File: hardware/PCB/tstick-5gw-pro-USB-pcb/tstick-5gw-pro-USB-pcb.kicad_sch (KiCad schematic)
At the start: 52 parts, among them J1 USB_C_Receptacle_USB2.0, J2 GPIO2, J3 GPIO1, Q2 20V/4.2A/52mOhm/1.4W, Q3 BSS138, SW1 JST-SH-1.00mm 1x2, SW2 PTS810 SJM Switch, U1 XC6222B331MR-G, U3 MCP73831-2-OT, U4 PCA9306DP

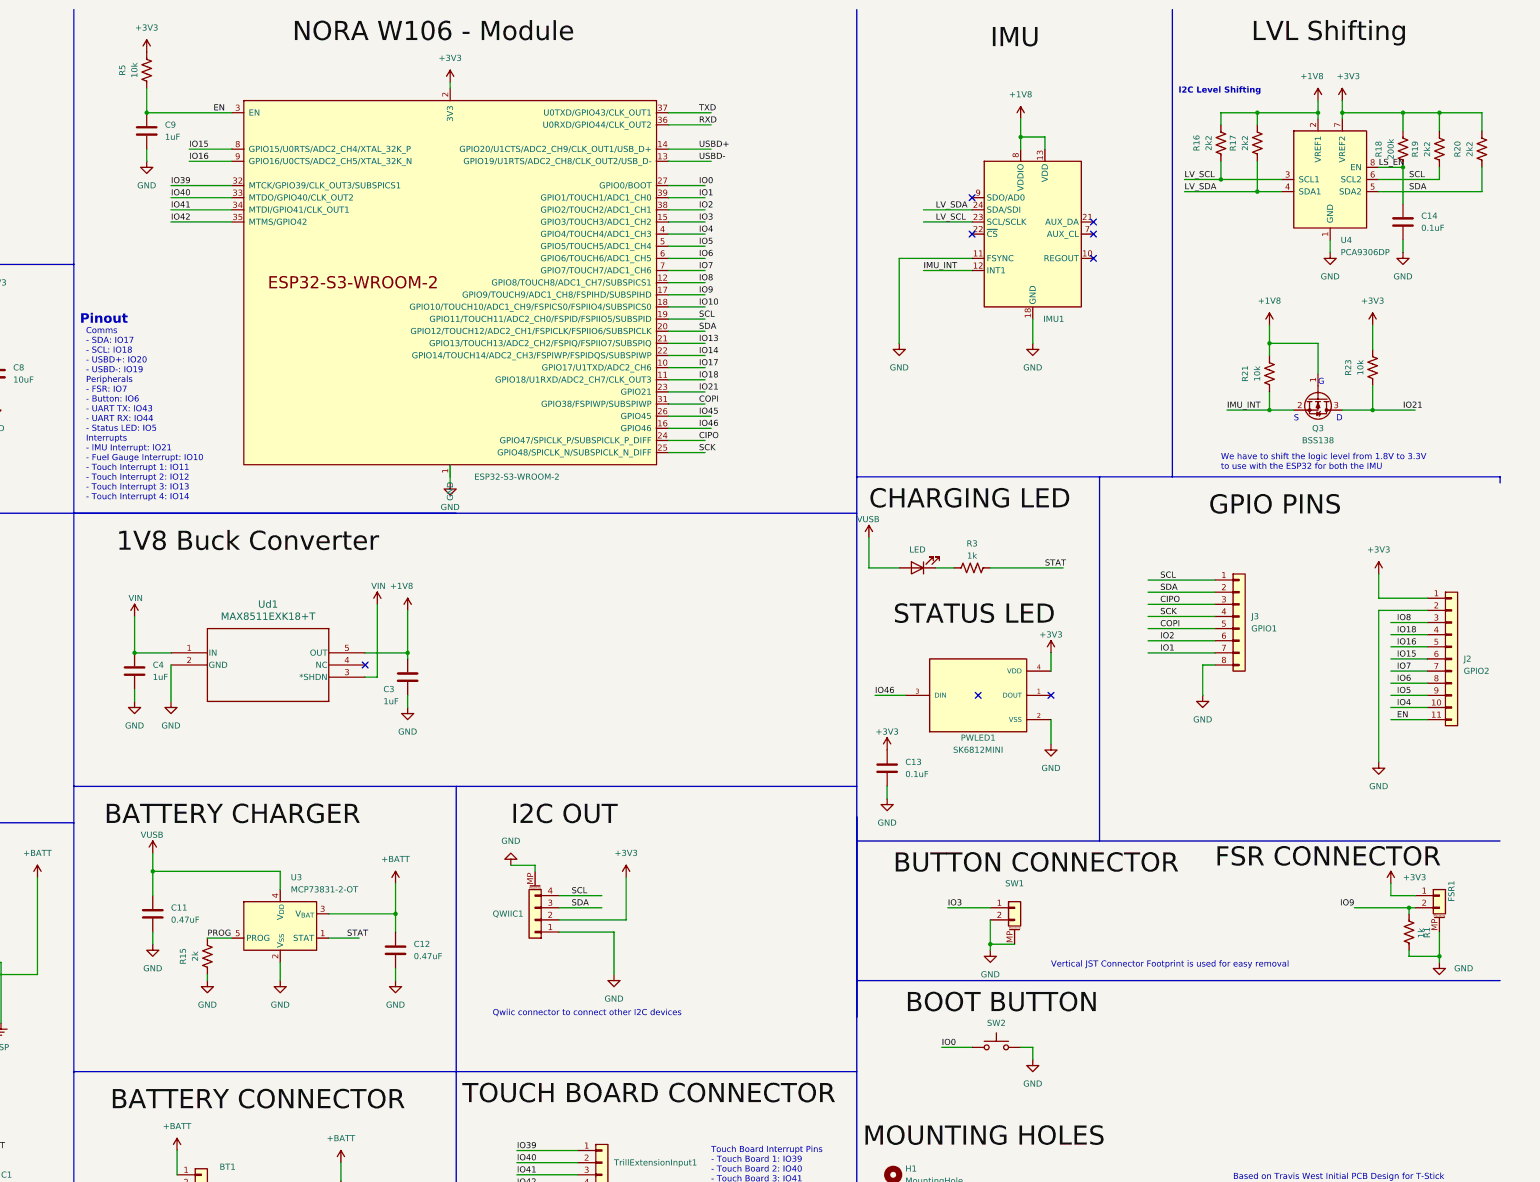
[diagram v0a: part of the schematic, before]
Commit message: completed usb only design
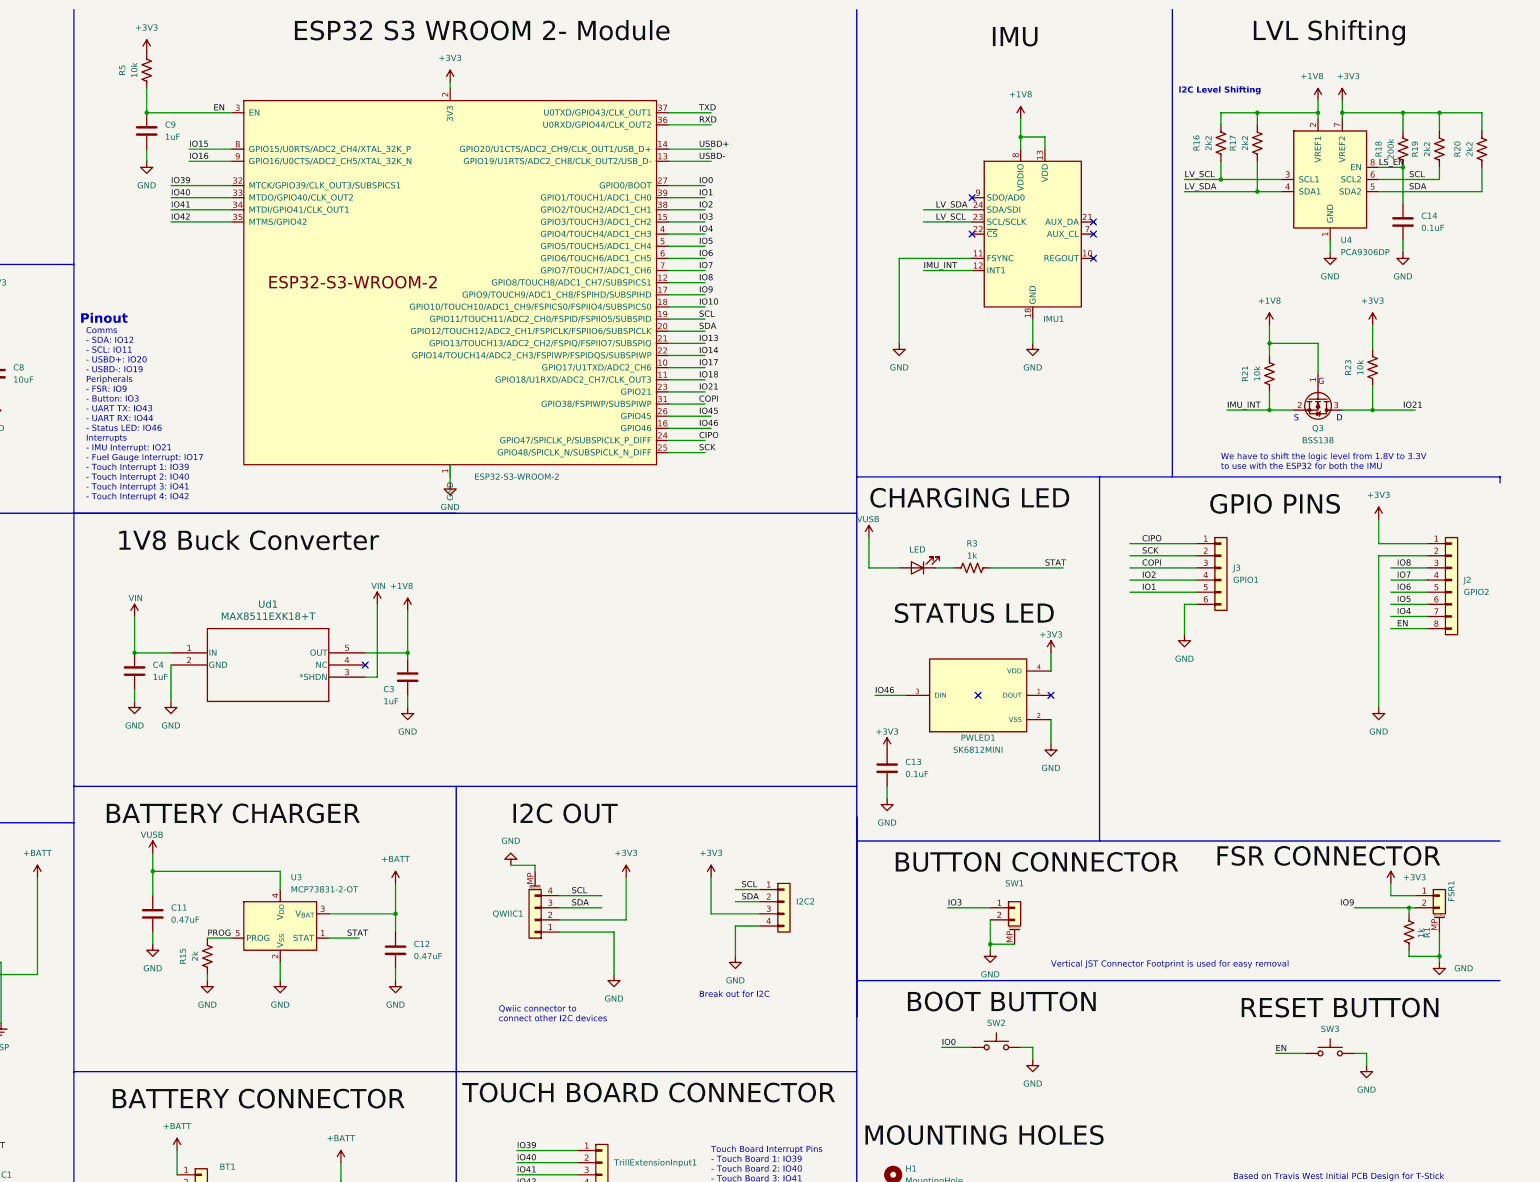
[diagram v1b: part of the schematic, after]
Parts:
- removed J2: GPIO2, Connector_PinHeader_2.54mm:PinHeader_1x11_P2.54mm_Vertical, symbol Connector_Generic:Conn_01x11
- removed J3: GPIO1, Connector_PinHeader_2.54mm:PinHeader_1x08_P2.54mm_Vertical, symbol Connector_Generic:Conn_01x08
- added I2C2: Conn_01x04, Connector_PinHeader_2.54mm:PinHeader_2x02_P2.54mm_Vertical, symbol Connector_Generic:Conn_01x04
- added J2: GPIO2, Connector_PinHeader_2.54mm:PinHeader_1x08_P2.54mm_Vertical, symbol Connector_Generic:Conn_01x08
- added J3: GPIO1, Connector_PinHeader_2.54mm:PinHeader_1x06_P2.54mm_Vertical, symbol Connector_Generic:Conn_01x06
- added SW3: PTS810 SJM Switch, Button_Switch_SMD:SW_SPST_PTS810, symbol Switch:SW_Push
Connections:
- net +3V3: now also I2C2.3 (Pin_3), J2.1 (Pin_1)
- net CIPO: now also J3.1 (Pin_1)
- net COPI: now also J3.3 (Pin_3)
- net EN: now also J2.8 (Pin_8), SW3.1
- net GND: now also I2C2.4 (Pin_4), J2.2 (Pin_2), J3.6 (Pin_6), SW3.2
- net IO1: now also J3.5 (Pin_5)
- net IO2: now also J3.4 (Pin_4)
- net IO4: now also J2.7 (Pin_7)
- net IO5: now also J2.6 (Pin_6)
- net IO6: now also J2.5 (Pin_5)
- net IO7: now also J2.4 (Pin_4)
- net IO8: now also J2.3 (Pin_3)
- net SCK: now also J3.2 (Pin_2)
- net SCL: now also I2C2.1 (Pin_1)
- net SDA: now also I2C2.2 (Pin_2)
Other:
- note added: "Break out for I2C"
- note added: "Comms - SDA: IO12 - SCL: IO11 - USBD+: IO20 - USBD-: IO19 Peripherals - FSR: IO9 - Button: IO3 - UART TX: IO43 - UART RX: IO44 - Status LED: IO46 Interrupts - IMU Interrupt: IO21 - Fuel Gauge Interrupt: IO17 - Touch Interrupt 1: IO39 - Touch Interrupt 2: IO40 - Touch Interrupt 3: IO41 - Touch Interrupt 4: IO42"
- note removed: "Comms - SDA: IO17 - SCL: IO18 - USBD+: IO20 - USBD-: IO19 Peripherals - FSR: IO7 - Button: IO6 - UART TX: IO43 - UART RX: IO44 - Status LED: IO5 Interrupts - IMU Interrupt: IO21 - Fuel Gauge Interrupt: IO10 - Touch Interrupt 1: IO11 - Touch Interrupt 2: IO12 - Touch Interrupt 3: IO13 - Touch Interrupt 4: IO14"

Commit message: updated BOM for 5gw board, updated silkscreen for touch board
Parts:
- BT2, I2C2, J2, J3: now left out of the parts list
- R21, R23: value 10k -> 2k2; Description Value Pkg 10 kOhms ±1% 0.05W, 1/20W Chip Resistor 0201 (0603 Metric) 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 -> 2.2 kOhms ±1% 0.05W, 1/20W Chip Resistor 0201 (0603 Metric)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; Digikey Part # P122414CT-ND -> P122832CT-ND; Mfg Part # ERJ-1GNF1002C -> ERJ-1GNF2201C
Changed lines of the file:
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@@
       (effects (font (size 1.27 1.27)))
     )
-    (property "Value" "10k" (at 358.14 88.9 90)
+    (property "Value" "2k2" (at 358.14 88.9 90)
       (effects (font (size 1.27 1.27)))
     )
@@
       (effects (font (size 1.27 1.27)) hide)
     )
-    (property "Digikey Part #" "P122414CT-ND" (at 360.68 88.9 90)
-      (effects (font (size 1.27 1.27)) hide)
-    )
-    (property "Description Value Pkg" "10 kOhms ±1% 0.05W, 1/20W Chip Resistor 0201 (0603 Metric) Thick Film" (at 360.68 88.9 0)
-      (effects (font (size 1.27 1.27)) hide)
-    )
-    (property "Mfg Part #" "ERJ-1GNF1002C" (at 360.68 88.9 0)
+    (property "Digikey Part #" "P122832CT-ND" (at 360.68 88.9 90)
+      (effects (font (size 1.27 1.27)) hide)
+    )
+    (property "Description Value Pkg" "2.2 kOhms ±1% 0.05W, 1/20W Chip Resistor 0201 (0603 Metric) Thick Film" (at 360.68 88.9 0)
+      (effects (font (size 1.27 1.27)) hide)
+    )
+    (property "Mfg Part #" "ERJ-1GNF2201C" (at 360.68 88.9 0)
       (effects (font (size 1.27 1.27)) hide)
     )
@@
   )
   (symbol (lib_id "Connector_Generic:Conn_01x04") (at 259.08 199.39 0) (unit 1)
-    (in_bom yes) (on_board yes) (dnp no) (fields_autoplaced)
+    (in_bom no) (on_board yes) (dnp no) (fields_autoplaced)
     (property "Reference" "I2C2" (at 261.62 199.39 0)
       (effects (font (size 1.27 1.27)) (justify left))
@@
   )
   (symbol (lib_id "Connector_Generic:Conn_01x06") (at 350.52 129.54 0) (unit 1)
-    (in_bom yes) (on_board yes) (dnp no) (fields_autoplaced)
+    (in_bom no) (on_board yes) (dnp no) (fields_autoplaced)
     (property "Reference" "J3" (at 353.06 129.54 0)
       (effects (font (size 1.27 1.27)) (justify left))
@@
   )
   (symbol (lib_id "Device:Battery_Cell") (at 166.37 262.89 0) (unit 1)
-    (in_bom yes) (on_board yes) (dnp no) (fields_autoplaced)
+    (in_bom no) (on_board yes) (dnp no) (fields_autoplaced)
     (property "Reference" "BT2" (at 170.18 259.7785 0)
       (effects (font (size 1.27 1.27)) (justify left))
@@
   )
   (symbol (lib_id "Connector_Generic:Conn_01x08") (at 398.78 132.08 0) (unit 1)
-    (in_bom yes) (on_board yes) (dnp no) (fields_autoplaced)
+    (in_bom no) (on_board yes) (dnp no) (fields_autoplaced)
     (property "Reference" "J2" (at 401.32 132.08 0)
       (effects (font (size 1.27 1.27)) (justify left))
@@
       (effects (font (size 1.27 1.27)))
     )
-    (property "Value" "10k" (at 379.73 87.63 90)
+    (property "Value" "2k2" (at 379.73 87.63 90)
       (effects (font (size 1.27 1.27)))
     )
@@
       (effects (font (size 1.27 1.27)) hide)
     )
-    (property "Digikey Part #" "P122414CT-ND" (at 382.27 87.63 90)
-      (effects (font (size 1.27 1.27)) hide)
-    )
-    (property "Description Value Pkg" "10 kOhms ±1% 0.05W, 1/20W Chip Resistor 0201 (0603 Metric) Thick Film" (at 382.27 87.63 0)
-      (effects (font (size 1.27 1.27)) hide)
-    )
-    (property "Mfg Part #" "ERJ-1GNF1002C" (at 382.27 87.63 0)
-      (effects (font (size 1.27 1.27)) hide)
-    )
+    (property "Digikey Part #" "P122832CT-ND" (at 382.27 87.63 90)
+      (effects (font (size 1.27 1.27)) hide)
+    )
+    (property "Description Value Pkg" "2.2 kOhms ±1% 0.05W, 1/20W Chip Resistor 0201 (0603 Metric) Thick Film" (at 382.27 87.63 0)
+      (effects (font (size 1.27 1.27)) hide)
+    )
+    (property "Mfg Part #" "ERJ-1GNF2201C" (at 382.27 87.63 0)
+      (effects (font (size 1.27 1.27)) hide)
+    )

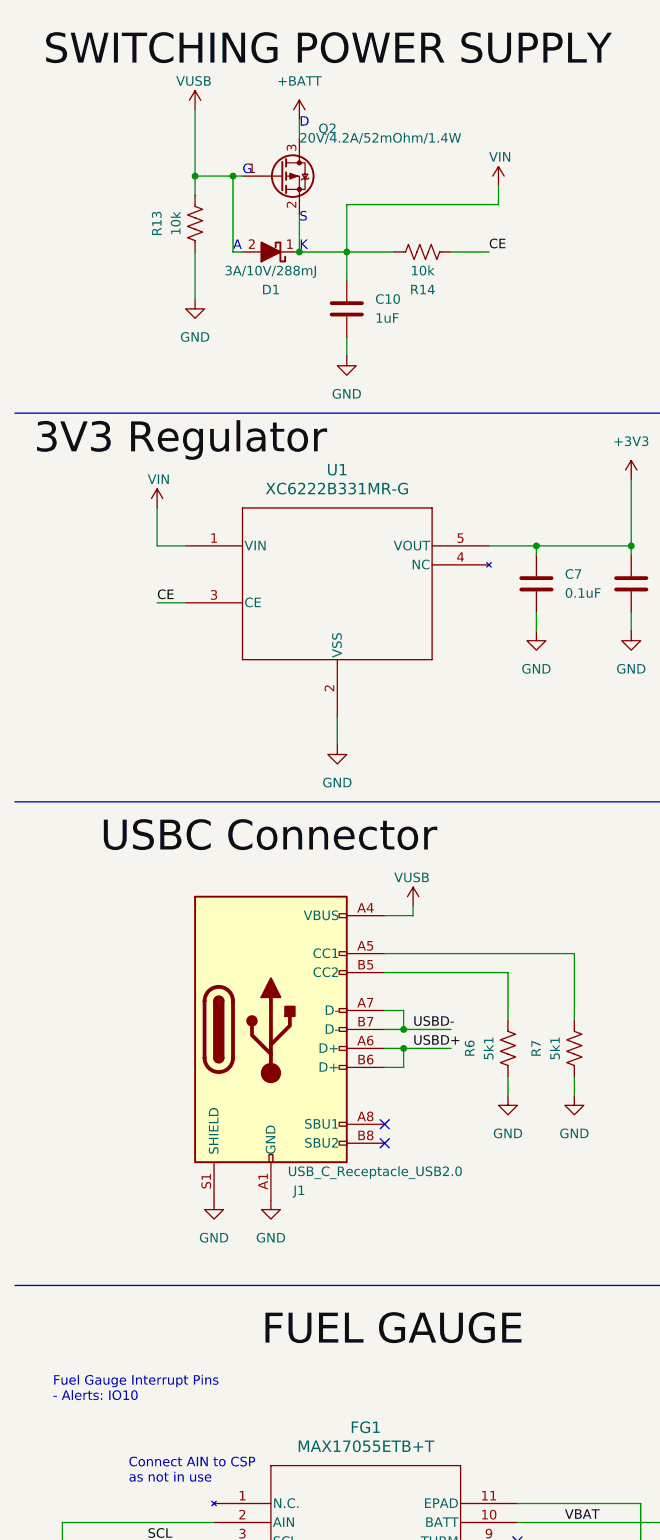
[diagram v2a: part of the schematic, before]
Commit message: update USB design
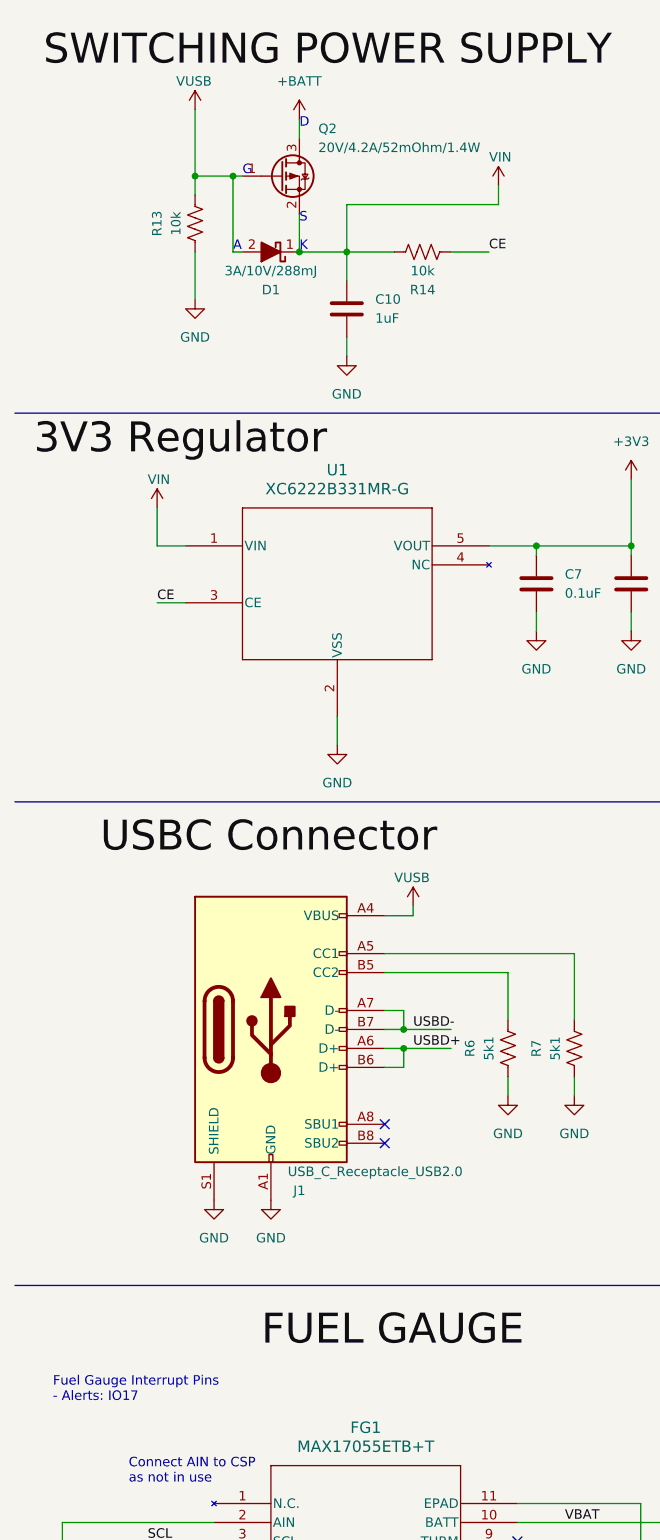
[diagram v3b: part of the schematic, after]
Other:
- note added: "Fuel Gauge Interrupt Pins - Alerts: IO17"
- note removed: "Fuel Gauge Interrupt Pins - Alerts: IO10"
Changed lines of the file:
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@@
     (effects (font (size 1.27 1.27)) (justify left bottom))
   )
-  (text "Fuel Gauge Interrupt Pins\n- Alerts: IO10\n\n" (at 16.51 200.66 0)
+  (text "Fuel Gauge Interrupt Pins\n- Alerts: IO17\n\n" (at 16.51 200.66 0)
     (effects (font (size 1.27 1.27)) (justify left bottom))
   )
@@
       (effects (font (size 1.27 1.27)) (justify left))
     )
-    (property "Value" "20V/4.2A/52mOhm/1.4W" (at 49.53 29.21 0)
-      (effects (font (size 1.27 1.27)) (justify left))
-    )
+    (property "Value" "20V/4.2A/52mOhm/1.4W" (at 52.07 30.48 0)
+      (effects (font (size 1.27 1.27)) (justify left))
+    )
